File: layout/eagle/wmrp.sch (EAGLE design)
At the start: 137 parts, among them IC1 ACS712, IC2 ADR392, IC3 ATMEGA32U4TQFP-44, IC4 AD8552, IC5 AD8552, Q1 BC817-40, Q2 BC817-40, Q3 IRF7416, Q4 IRF7413, Q5 BC817-40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

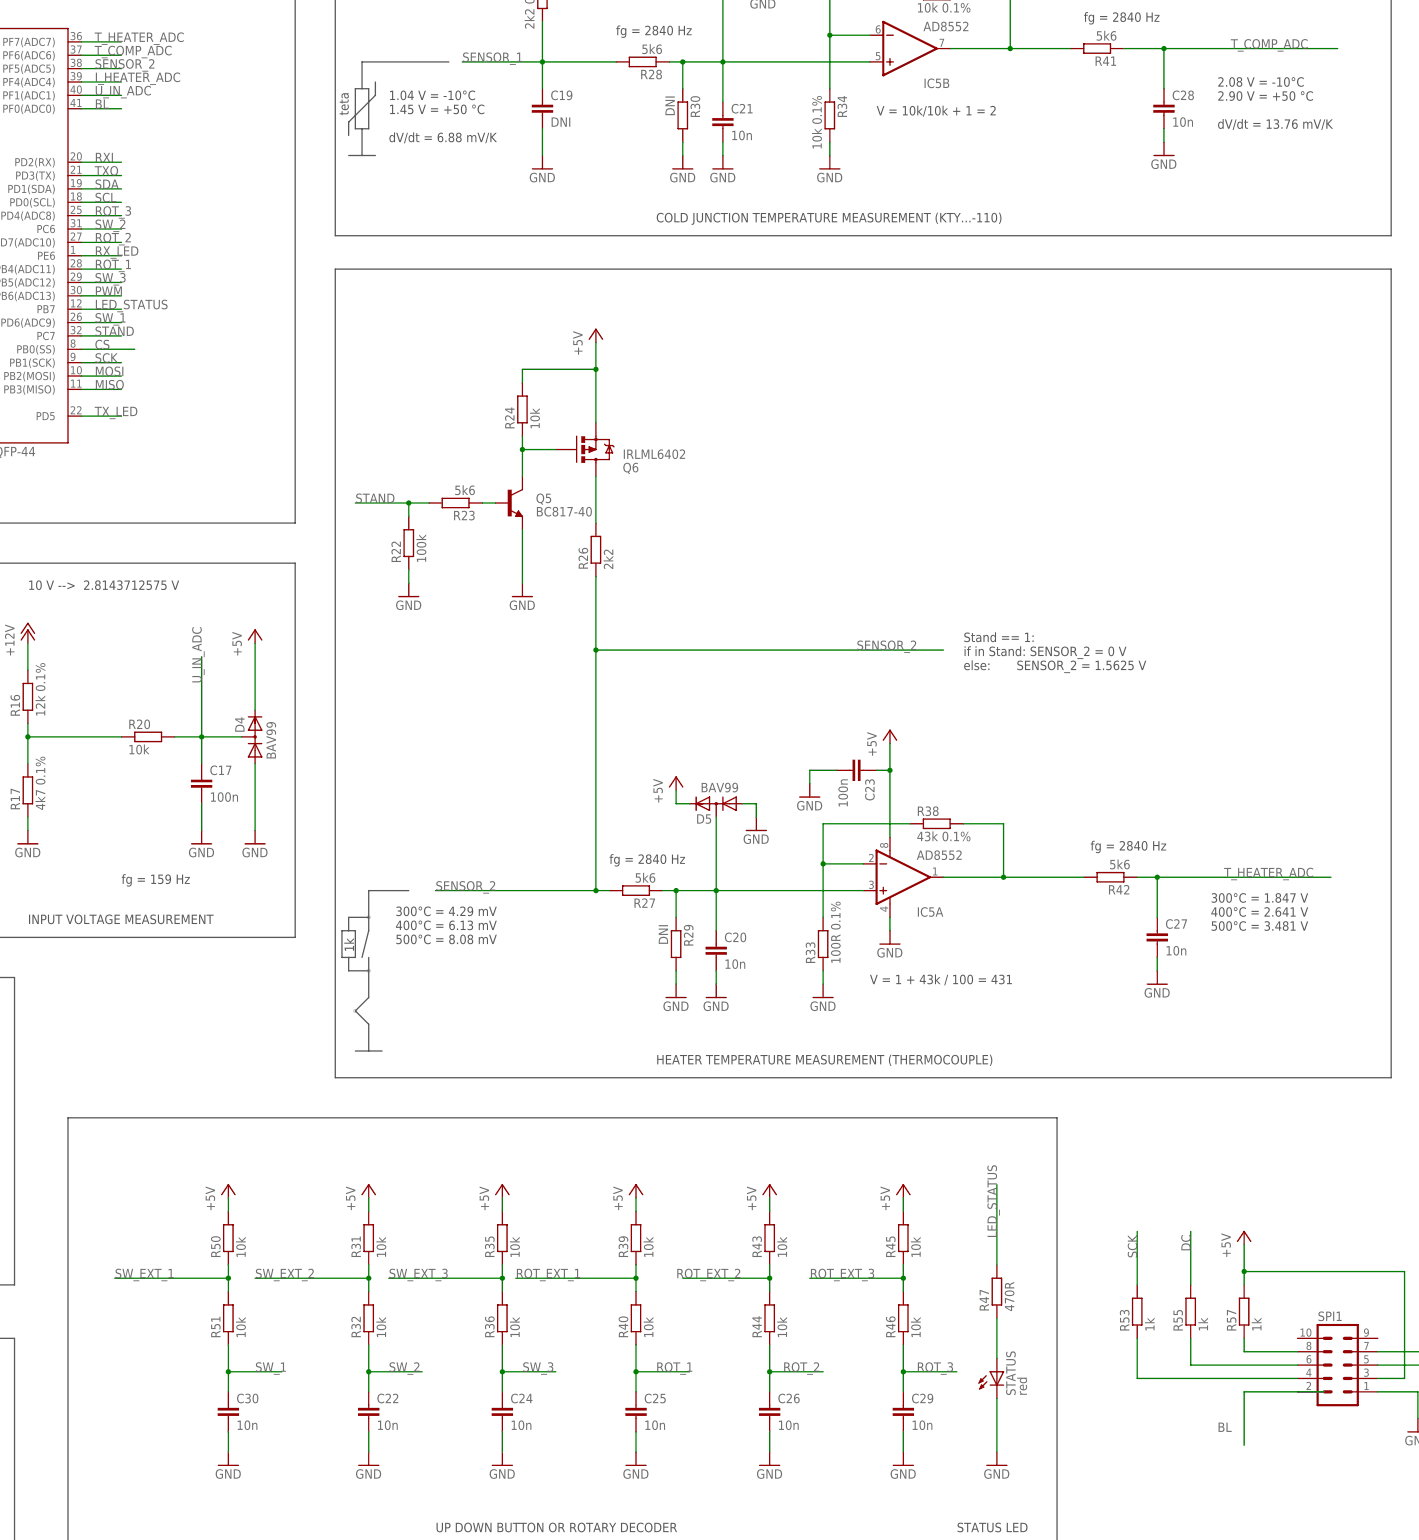
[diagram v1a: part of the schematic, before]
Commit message: Added SPI header with resistors to schematic and made connections on PCB
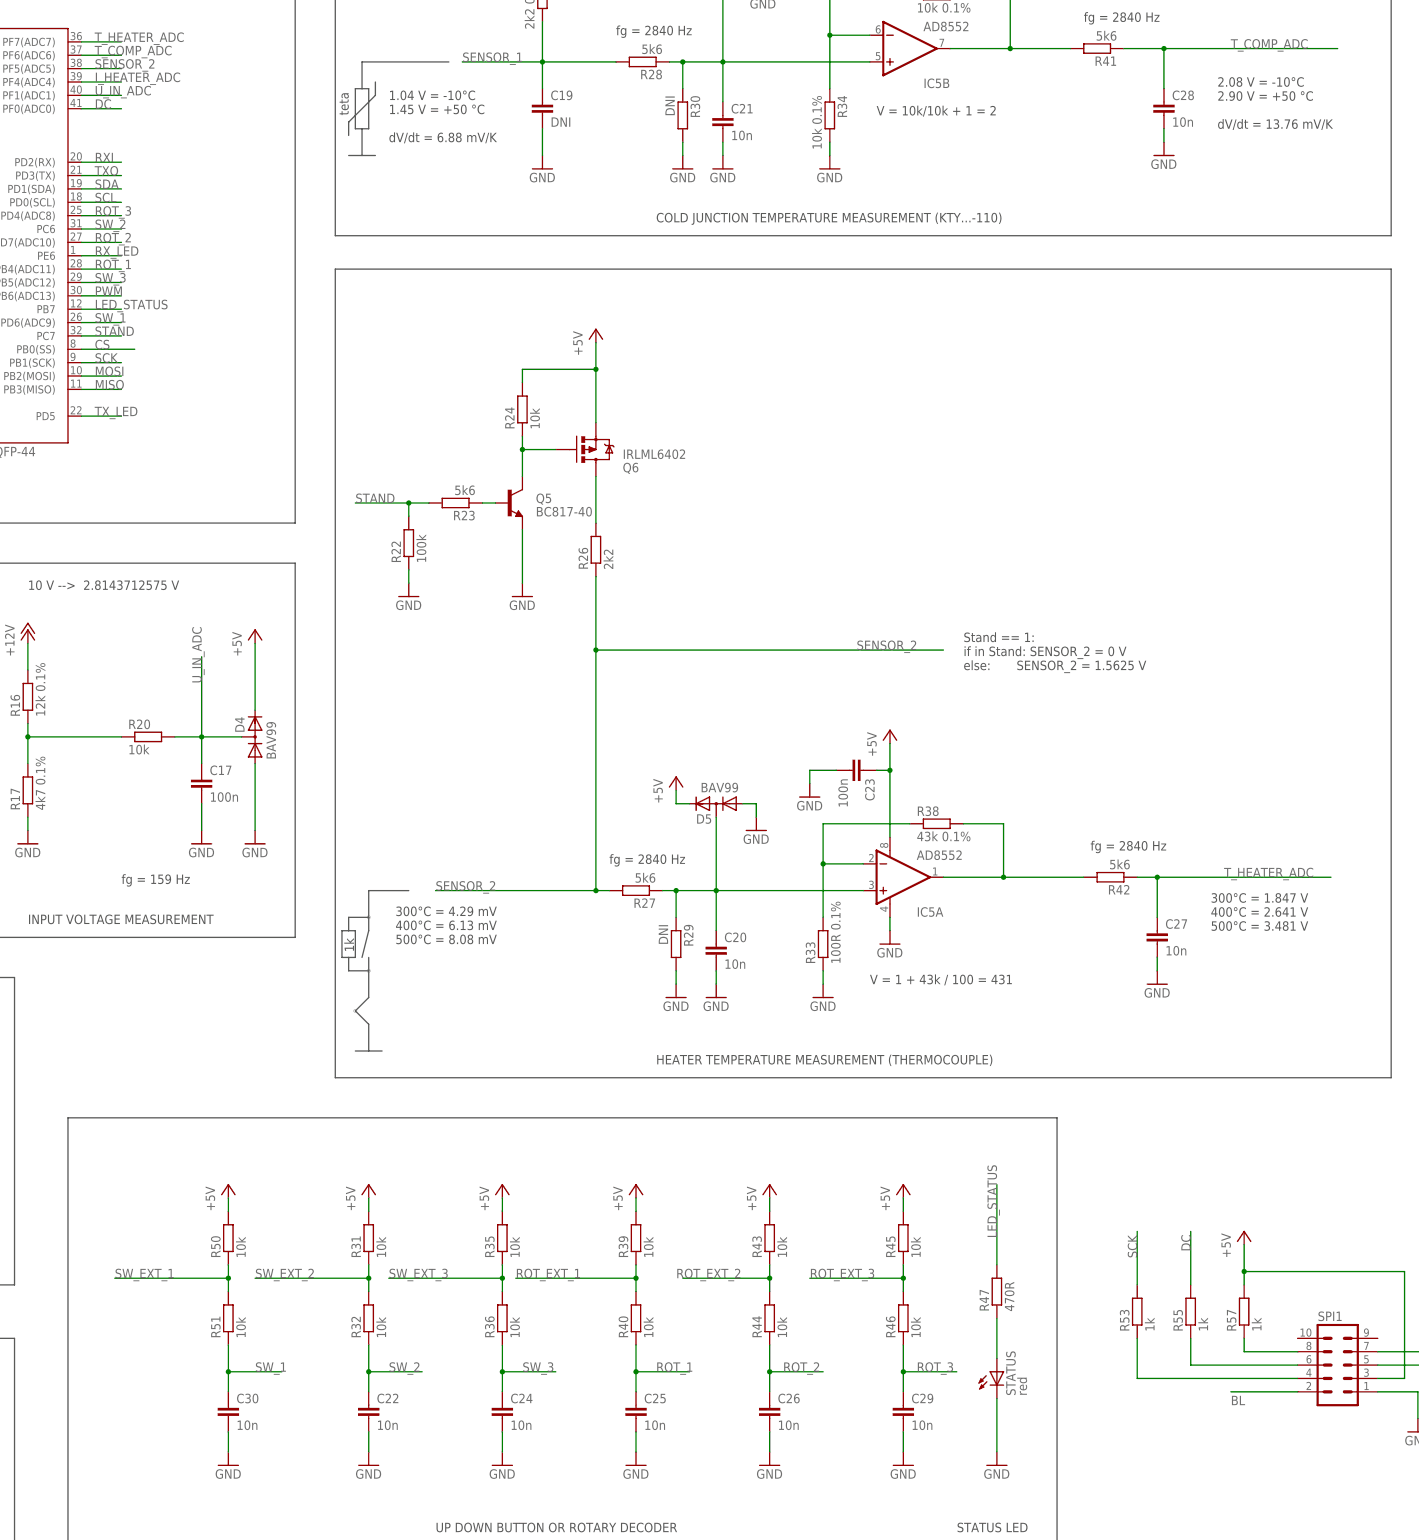
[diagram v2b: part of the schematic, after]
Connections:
- net BL: no longer IC3.PF0(ADC0)
- net DC: now also IC3.PF0(ADC0)
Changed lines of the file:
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@@
 <segment>
 <pinref part="SPI1" gate="G$1" pin="2"/>
-<wire x1="416.56" y1="5.08" x2="411.48" y2="5.08" width="0.1524" layer="91"/>
-<wire x1="411.48" y1="5.08" x2="401.32" y2="5.08" width="0.1524" layer="91"/>
-<wire x1="401.32" y1="5.08" x2="401.32" y2="-5.08" width="0.1524" layer="91"/>
-<label x="396.24" y="-2.54" size="1.778" layer="95"/>
-</segment>
-<segment>
-<pinref part="IC3" gate="G$1" pin="PF0(ADC0)"/>
-<wire x1="180.34" y1="248.92" x2="187.96" y2="248.92" width="0.1524" layer="91"/>
-<label x="182.88" y="248.92" size="1.778" layer="95"/>
+<wire x1="411.48" y1="5.08" x2="398.78" y2="5.08" width="0.1524" layer="91"/>
+<label x="398.78" y="2.54" size="1.778" layer="95"/>
 </segment>
 </net>
@@
 <label x="391.16" y="31.75" size="1.778" layer="95" rot="R90"/>
 </segment>
+<segment>
+<pinref part="IC3" gate="G$1" pin="PF0(ADC0)"/>
+<wire x1="180.34" y1="248.92" x2="187.96" y2="248.92" width="0.1524" layer="91"/>
+<label x="182.88" y="248.92" size="1.778" layer="95"/>
+</segment>
 </net>
